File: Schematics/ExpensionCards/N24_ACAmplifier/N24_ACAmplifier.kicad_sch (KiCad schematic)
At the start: 114 parts

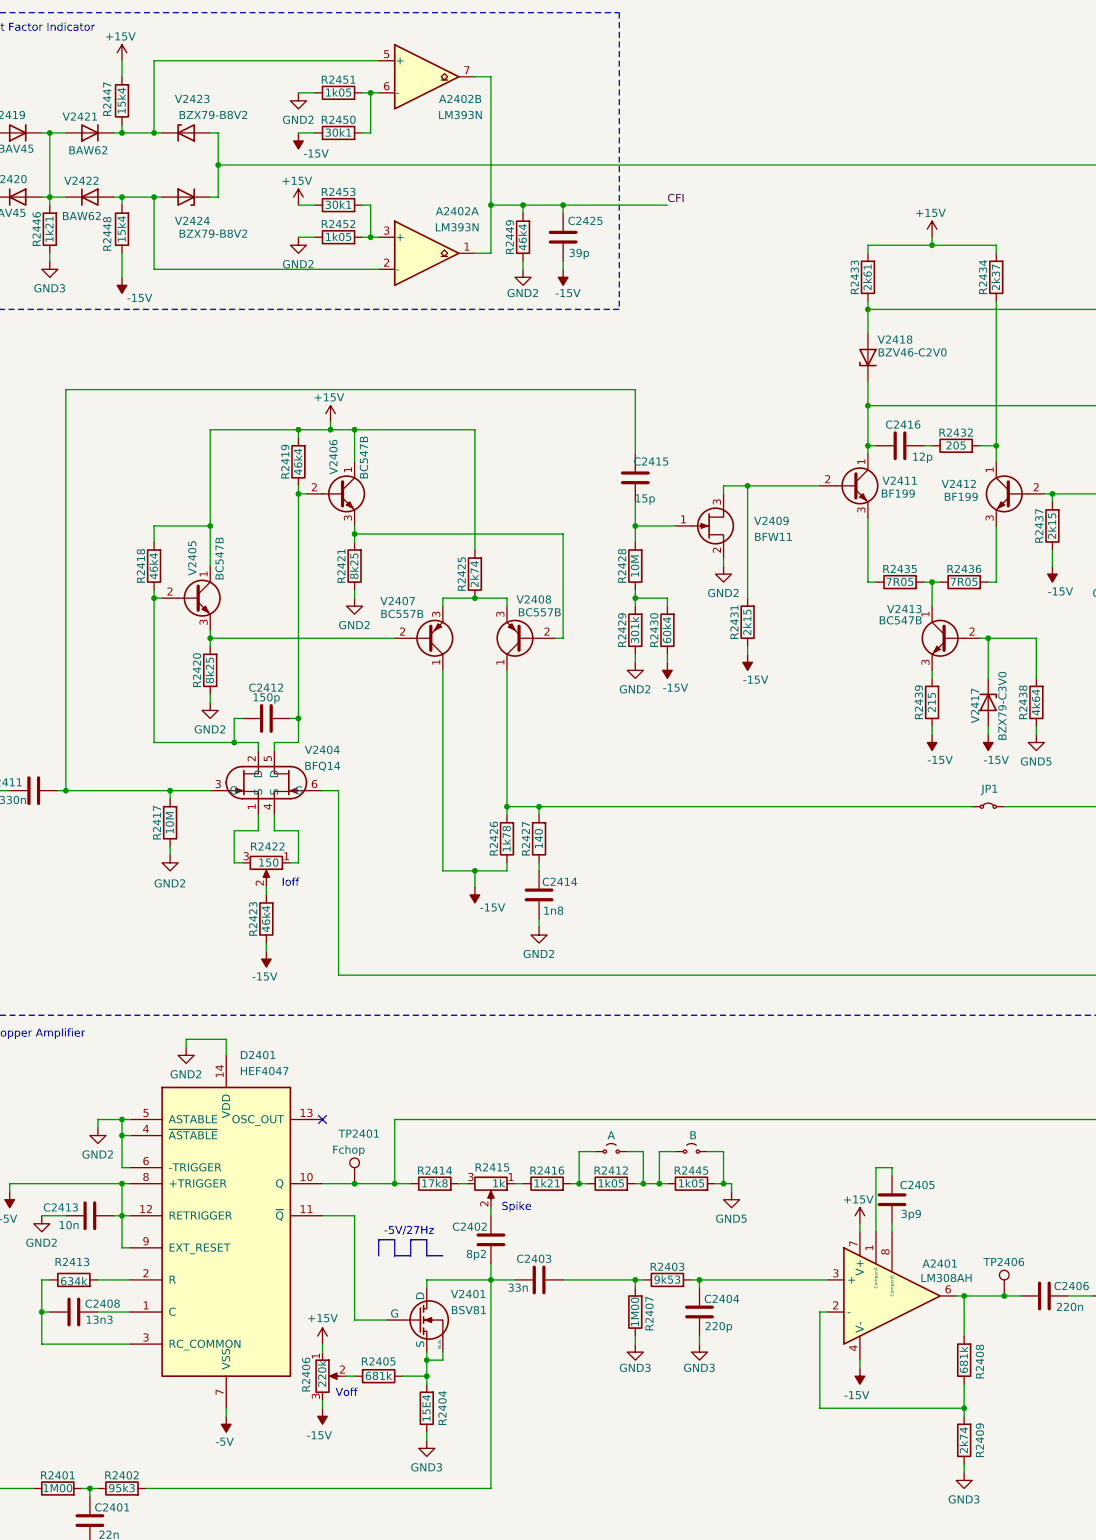
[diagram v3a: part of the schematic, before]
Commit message: Updated some component-values
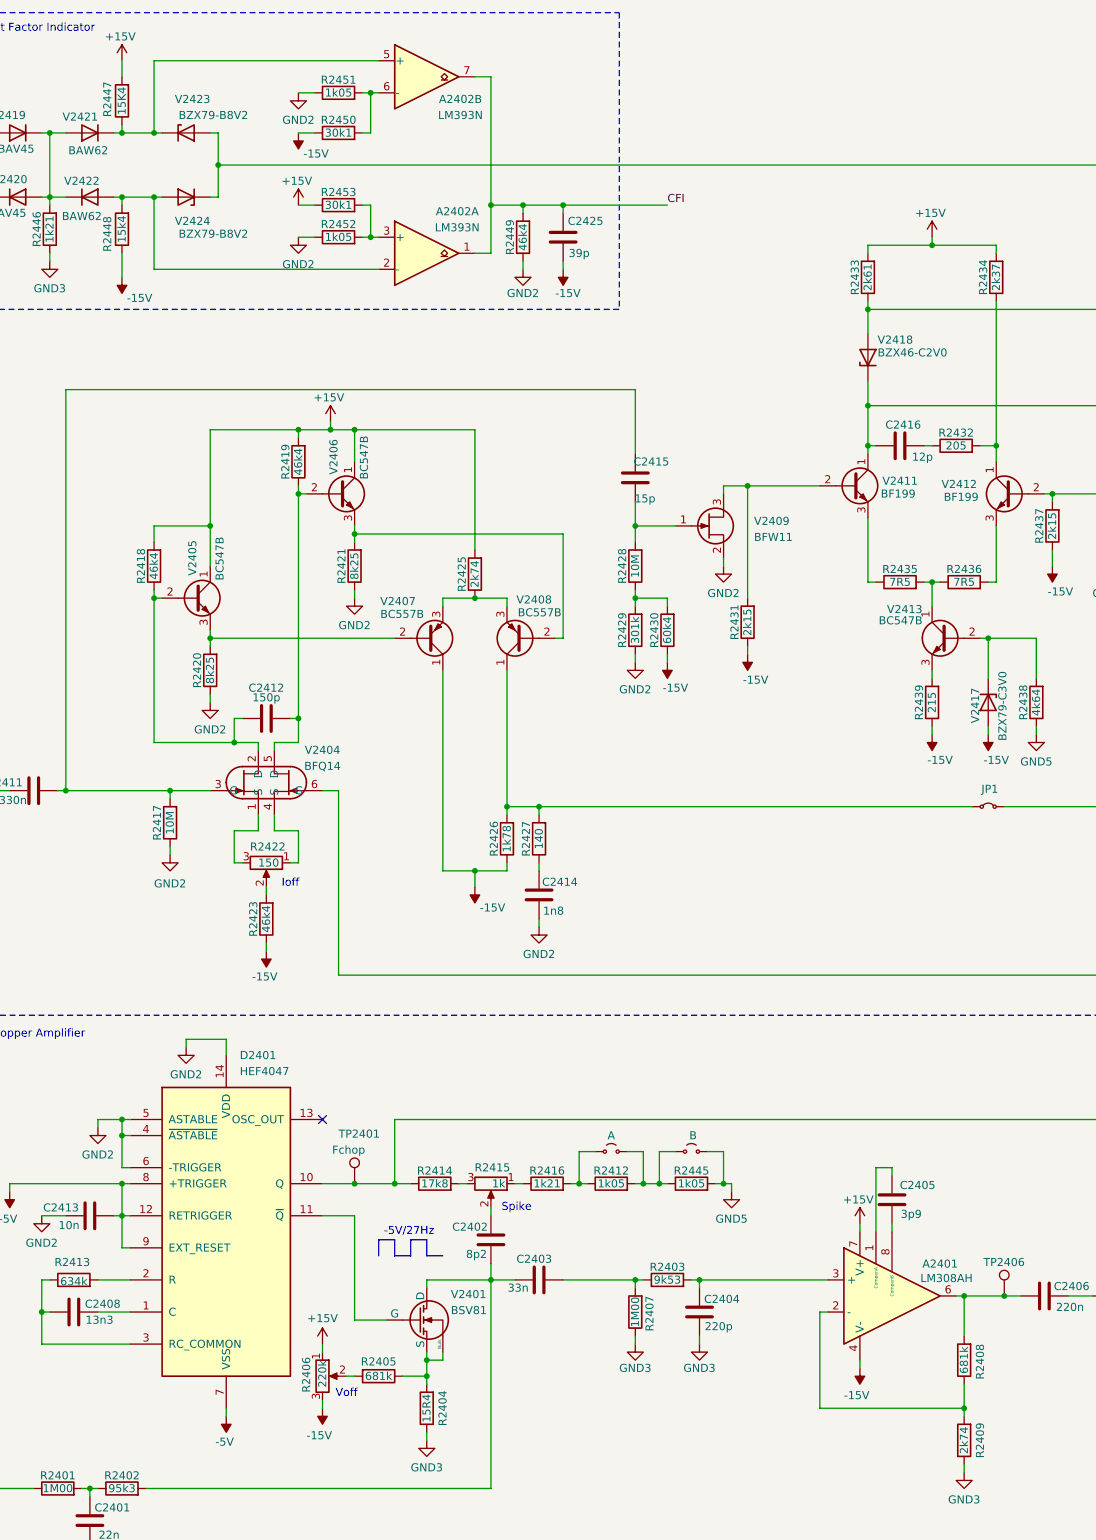
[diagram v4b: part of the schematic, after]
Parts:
- R2404: value 15E4 -> 15R4
- R2435, R2436: value 7R05 -> 7R5
- R2447: value 15k4 -> 15K4
- V2418: value BZV46-C2V0 -> BZX46-C2V0
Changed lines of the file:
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@@
 	(title_block
 		(title "Philips PM2528 - N24 (AC Amplifier)")
-		(date "2025-08-15")
+		(date "2025-08-17")
 		(rev "0.1")
 		(company "D. Kupers")
@@
 			)
 		)
-		(property "Value" "BZV46-C2V0"
+		(property "Value" "BZX46-C2V0"
 			(at 221.234 67.818 90)
 			(effects
@@
 			)
 		)
-		(property "Value" "7R05"
+		(property "Value" "7R5"
 			(at 234.95 104.14 90)
 			(effects
@@
 			)
 		)
-		(property "Value" "15k4"
+		(property "Value" "15K4"
 			(at 101.6 27.94 90)
 			(effects
@@
 			)
 		)
-		(property "Value" "15E4"
+		(property "Value" "15R4"
 			(at 149.86 234.95 90)
 			(effects
@@
 			)
 		)
-		(property "Value" "7R05"
+		(property "Value" "7R5"
 			(at 224.79 104.14 90)
 			(effects
